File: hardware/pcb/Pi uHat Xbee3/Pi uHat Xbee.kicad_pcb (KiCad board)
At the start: 2 copper layers, 65 x 30.5 mm, 19 parts, among them J1 Conn_01x02, J2 RPi_GPIO, J3 Conn_01x01, J4 Conn_01x01, J5 Conn_01x01, J6 Conn_01x01, J7 Conn_01x01, U1 XBee3

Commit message: Hat Pi Wbee fini
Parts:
- added G***: LOGO, Insa:insa-image, F.Cu at (73.7, 39.4)
- moved R2 46.2 mm to (64.1, 45.7), turned to 270 degrees
- moved D3 42.3 mm to (67.9, 51.4), turned to 90 degrees
- moved R3 37.4 mm to (67.9, 45.7), turned to 270 degrees
- moved R1 36.4 mm to (60.3, 45.7), turned to 270 degrees
- moved D1 35.3 mm to (60.3, 51.4), turned to 90 degrees
- moved D2 33.8 mm to (64.1, 51.4), turned to 90 degrees
- moved J1 23.9 mm to (21.3, 36.6)
- moved J7 19.9 mm to (26.7, 42.5)
- moved C1 12.9 mm to (21.3, 42.7), turned to 270 degrees
- moved J3 10.5 mm to (26.7, 37.5)
- moved J6 10.3 mm to (26.7, 33.0)
- moved J4 8.31 mm to (26.7, 51.4)
- moved J5 7.38 mm to (26.7, 47.0)
- moved U1 6.43 mm to (43.2, 40.6), turned to 0 degrees
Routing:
- net GND: track 0.00 -> 153.5 mm
- net /ASSOCIATE: track 0.00 -> 105.5 mm
- net /~SLEEP: track 0.00 -> 58.3 mm, vias 0 -> 2
- net /SLEEP_REQ: track 0.00 -> 31.3 mm
- net /RSSI_PWM: track 0.00 -> 27.5 mm
- net /DIN: track 0.00 -> 25.2 mm
- net /~RESET: track 0.00 -> 24.8 mm
- net Net-(J2-Pad33): track 0.00 -> 20.3 mm
- net Net-(J2-Pad31): track 0.00 -> 19.0 mm
- net Net-(J2-Pad29): track 0.00 -> 17.8 mm
- net Net-(C1-Pad1): track 0.00 -> 16.2 mm
- net /DOUT: track 0.00 -> 13.0 mm
- net VDD: track 0.00 -> 5.08 mm
- net Net-(D3-Pad2): track 0.00 -> 2.68 mm
- net Net-(D2-Pad2): track 0.00 -> 2.68 mm
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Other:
- board text added: "06/01/2022"
- board text added: "Hat Xbee"
- board text added: "Idd XBEE"
- board text added: "Ver 1.0"

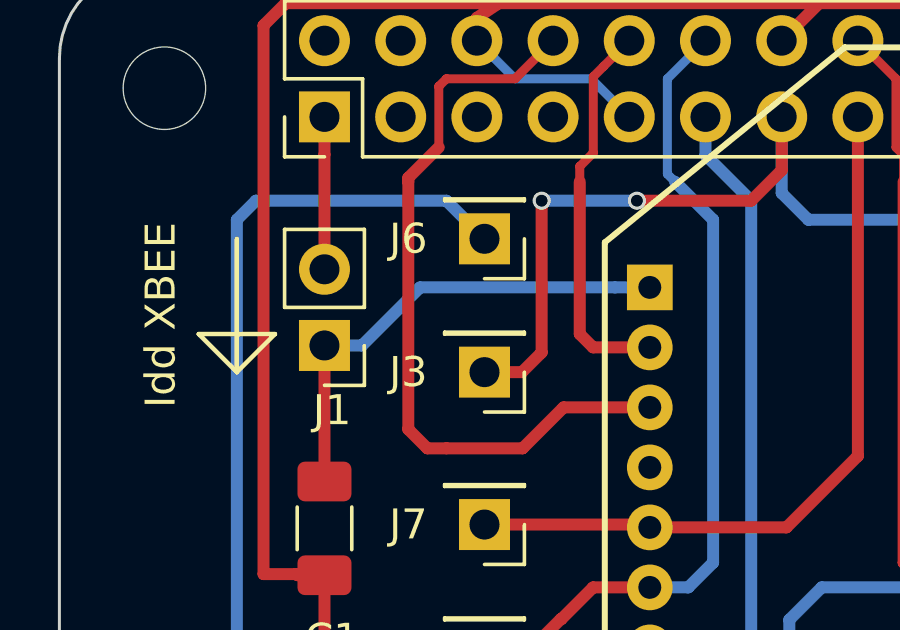
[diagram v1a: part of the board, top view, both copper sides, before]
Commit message: reorganisation de l'arborescence + renommage serveré
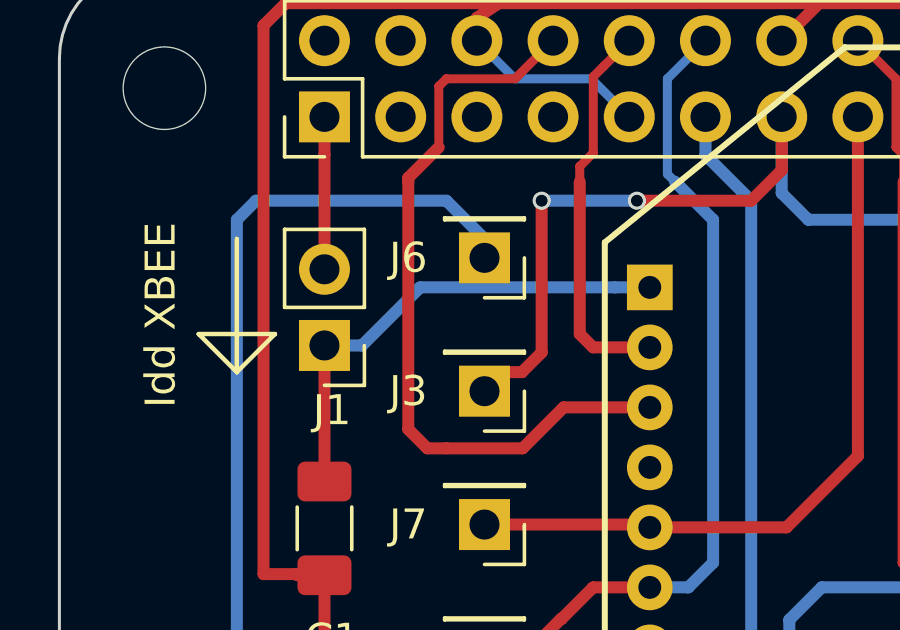
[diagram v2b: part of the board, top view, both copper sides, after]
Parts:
- moved J3 0.63 mm to (26.7, 38.1)
- moved J6 0.63 mm to (26.7, 33.7)
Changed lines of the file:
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@@
   )
   (setup
-    (last_trace_width 0.4)
+    (last_trace_width 0.25)
     (user_trace_width 0.2)
     (user_trace_width 0.25)
@@
     (add_net "Net-(J2-Pad33)")
     (add_net VDD)
+  )
+  (module Insa:Xbee3 locked (layer F.Cu)
+    (at 43.18 40.64)
+    (fp_text reference U1 (at 13.335 -8.89) (layer F.SilkS)
+      (effects (font (size 1 1) (thickness 0.15)))
+    )
+    (fp_text value XBee3 (at 0 6.5) (layer F.Fab)
+      (effects (font (size 1 1) (thickness 0.15)))
+    )
+    (fp_line (start -12.5 -7.5) (end -4.5 -14) (layer F.CrtYd) (width 0.2))
+    (fp_line (start -12.5 13.5) (end -12.5 -7.5) (layer F.CrtYd) (width 0.2))
+    (fp_line (start 12.5 13.5) (end -12.5 13.5) (layer F.CrtYd) (width 0.2))
+    (fp_line (start 12.5 -7.5) (end 12.5 13.5) (layer F.CrtYd) (width 0.2))
+    (fp_line (start 4.5 -14) (end 12.5 -7.5) (layer F.CrtYd) (width 0.2))
+    (fp_line (start -4.5 -14) (end 4.5 -14) (layer F.CrtYd) (width 0.2))
+    (fp_line (start -12.5 -7.5) (end -4.5 -14) (layer F.SilkS) (width 0.2))
+    (fp_line (start 4.5 -14) (end 12.5 -7.5) (layer F.SilkS) (width 0.2))
+    (fp_line (start -4.5 -14) (end 4.5 -14) (layer F.SilkS) (width 0.2))
+    (fp_line (start -12.5 13.5) (end -12.5 -7.5) (layer F.SilkS) (width 0.2))
+    (fp_line (start 12.5 13.5) (end 12.5 -7.5) (layer F.SilkS) (width 0.2))
+    (fp_line (start -12.5 13.5) (end 12.5 13.5) (layer F.SilkS) (width 0.2))
+    (pad 10 thru_hole circle (at -11 12) (size 1.524 1.524) (drill 0.762) (layers *.Cu *.Mask)
+      (net 4 GND))
+    (pad 9 thru_hole circle (at -11 10) (size 1.524 1.524) (drill 0.762) (layers *.Cu *.Mask)
+      (net 11 /SLEEP_REQ))
+    (pad 8 thru_hole circle (at -11 8) (size 1.524 1.524) (drill 0.762) (layers *.Cu *.Mask))
+    (pad 7 thru_hole circle (at -11 6) (size 1.524 1.524) (drill 0.762) (layers *.Cu *.Mask))
+    (pad 6 thru_hole circle (at -11 4) (size 1.524 1.524) (drill 0.762) (layers *.Cu *.Mask)
+      (net 12 /RSSI_PWM))
+    (pad 5 thru_hole circle (at -11 2) (size 1.524 1.524) (drill 0.762) (layers *.Cu *.Mask)
+      (net 14 /~RESET))
+    (pad 11 thru_hole circle (at 11 12) (size 1.524 1.524) (drill 0.762) (layers *.Cu *.Mask))
+    (pad 12 thru_hole circle (at 11 10) (size 1.524 1.524) (drill 0.762) (layers *.Cu *.Mask))
+    (pad 13 thru_hole circle (at 11 8) (size 1.524 1.524) (drill 0.762) (layers *.Cu *.Mask)
+      (net 10 /~SLEEP))
+    (pad 14 thru_hole circle (at 11 6) (size 1.524 1.524) (drill 0.762) (layers *.Cu *.Mask))
+    (pad 15 thru_hole circle (at 11 4) (size 1.524 1.524) (drill 0.762) (layers *.Cu *.Mask)
+      (net 13 /ASSOCIATE))
+    (pad 16 thru_hole circle (at 11 2) (size 1.524 1.524) (drill 0.762) (layers *.Cu *.Mask))
+    (pad 20 thru_hole circle (at 11 -6) (size 1.524 1.524) (drill 0.762) (layers *.Cu *.Mask)
+      (net 4 GND))
+    (pad 19 thru_hole circle (at 11 -4) (size 1.524 1.524) (drill 0.762) (layers *.Cu *.Mask)
+      (net 4 GND))
+    (pad 18 thru_hole circle (at 11 -2) (size 1.524 1.524) (drill 0.762) (layers *.Cu *.Mask)
+      (net 4 GND))
+    (pad 1 thru_hole rect (at -11 -6) (size 1.524 1.524) (drill 0.762) (layers *.Cu *.Mask)
+      (net 5 "Net-(C1-Pad1)"))
+    (pad 2 thru_hole circle (at -11 -4) (size 1.524 1.524) (drill 0.762) (layers *.Cu *.Mask)
+      (net 15 /DOUT))
+    (pad 3 thru_hole circle (at -11 -2) (size 1.524 1.524) (drill 0.762) (layers *.Cu *.Mask)
+      (net 16 /DIN))
+    (pad 17 thru_hole circle (at 11 0) (size 1.524 1.524) (drill 0.762) (layers *.Cu *.Mask)
+      (net 4 GND))
+    (pad 4 thru_hole circle (at -11 0) (size 1.524 1.524) (drill 0.762) (layers *.Cu *.Mask))
+    (model /home/dimercur/kicad/local-packages3d/Insa.3dshapes/XBee_Module_-_ZB_Series_S2C_-_2mW_with_Wire_Antenna_-_XB24CZ7WIT-004_1661764185.214.step
+      (offset (xyz 0 -13.9192 6.680200000000001))
+      (scale (xyz 1 1 1))
+      (rotate (xyz 0 -180 0))
+    )
   )
   (module Insa:insa-image (layer F.Cu)
@@
     )
   )
-  (module Insa:Xbee3 locked (layer F.Cu)
-    (at 43.18 40.64)
-    (fp_text reference U1 (at 13.335 -8.89) (layer F.SilkS)
-      (effects (font (size 1 1) (thickness 0.15)))
-    )
-    (fp_text value XBee3 (at 0 6.5) (layer F.Fab)
-      (effects (font (size 1 1) (thickness 0.15)))
-    )
-    (fp_line (start -12.5 -7.5) (end -4.5 -14) (layer F.CrtYd) (width 0.2))
-    (fp_line (start -12.5 13.5) (end -12.5 -7.5) (layer F.CrtYd) (width 0.2))
-    (fp_line (start 12.5 13.5) (end -12.5 13.5) (layer F.CrtYd) (width 0.2))
-    (fp_line (start 12.5 -7.5) (end 12.5 13.5) (layer F.CrtYd) (width 0.2))
-    (fp_line (start 4.5 -14) (end 12.5 -7.5) (layer F.CrtYd) (width 0.2))
-    (fp_line (start -4.5 -14) (end 4.5 -14) (layer F.CrtYd) (width 0.2))
-    (fp_line (start -12.5 -7.5) (end -4.5 -14) (layer F.SilkS) (width 0.2))
-    (fp_line (start 4.5 -14) (end 12.5 -7.5) (layer F.SilkS) (width 0.2))
-    (fp_line (start -4.5 -14) (end 4.5 -14) (layer F.SilkS) (width 0.2))
-    (fp_line (start -12.5 13.5) (end -12.5 -7.5) (layer F.SilkS) (width 0.2))
-    (fp_line (start 12.5 13.5) (end 12.5 -7.5) (layer F.SilkS) (width 0.2))
-    (fp_line (start -12.5 13.5) (end 12.5 13.5) (layer F.SilkS) (width 0.2))
-    (pad 10 thru_hole circle (at -11 12) (size 1.524 1.524) (drill 0.762) (layers *.Cu *.Mask)
-      (net 4 GND))
-    (pad 9 thru_hole circle (at -11 10) (size 1.524 1.524) (drill 0.762) (layers *.Cu *.Mask)
-      (net 11 /SLEEP_REQ))
-    (pad 8 thru_hole circle (at -11 8) (size 1.524 1.524) (drill 0.762) (layers *.Cu *.Mask))
-    (pad 7 thru_hole circle (at -11 6) (size 1.524 1.524) (drill 0.762) (layers *.Cu *.Mask))
-    (pad 6 thru_hole circle (at -11 4) (size 1.524 1.524) (drill 0.762) (layers *.Cu *.Mask)
-      (net 12 /RSSI_PWM))
-    (pad 5 thru_hole circle (at -11 2) (size 1.524 1.524) (drill 0.762) (layers *.Cu *.Mask)
-      (net 14 /~RESET))
-    (pad 11 thru_hole circle (at 11 12) (size 1.524 1.524) (drill 0.762) (layers *.Cu *.Mask))
-    (pad 12 thru_hole circle (at 11 10) (size 1.524 1.524) (drill 0.762) (layers *.Cu *.Mask))
-    (pad 13 thru_hole circle (at 11 8) (size 1.524 1.524) (drill 0.762) (layers *.Cu *.Mask)
-      (net 10 /~SLEEP))
-    (pad 14 thru_hole circle (at 11 6) (size 1.524 1.524) (drill 0.762) (layers *.Cu *.Mask))
-    (pad 15 thru_hole circle (at 11 4) (size 1.524 1.524) (drill 0.762) (layers *.Cu *.Mask)
-      (net 13 /ASSOCIATE))
-    (pad 16 thru_hole circle (at 11 2) (size 1.524 1.524) (drill 0.762) (layers *.Cu *.Mask))
-    (pad 20 thru_hole circle (at 11 -6) (size 1.524 1.524) (drill 0.762) (layers *.Cu *.Mask)
-      (net 4 GND))
-    (pad 19 thru_hole circle (at 11 -4) (size 1.524 1.524) (drill 0.762) (layers *.Cu *.Mask)
-      (net 4 GND))
-    (pad 18 thru_hole circle (at 11 -2) (size 1.524 1.524) (drill 0.762) (layers *.Cu *.Mask)
-      (net 4 GND))
-    (pad 1 thru_hole rect (at -11 -6) (size 1.524 1.524) (drill 0.762) (layers *.Cu *.Mask)
-      (net 5 "Net-(C1-Pad1)"))
-    (pad 2 thru_hole circle (at -11 -4) (size 1.524 1.524) (drill 0.762) (layers *.Cu *.Mask)
-      (net 15 /DOUT))
-    (pad 3 thru_hole circle (at -11 -2) (size 1.524 1.524) (drill 0.762) (layers *.Cu *.Mask)
-      (net 16 /DIN))
-    (pad 17 thru_hole circle (at 11 0) (size 1.524 1.524) (drill 0.762) (layers *.Cu *.Mask)
-      (net 4 GND))
-    (pad 4 thru_hole circle (at -11 0) (size 1.524 1.524) (drill 0.762) (layers *.Cu *.Mask))
-    (model "/home/dimercur/kicad/local-packages3d/Insa.3dshapes/XBee Pro 60mW.STEP"
-      (offset (xyz -2 7.5 8))
-      (scale (xyz 1 1 1))
-      (rotate (xyz -90 0 -90))
-    )
-  )
   (module Resistor_SMD:R_1206_3216Metric_Pad1.30x1.75mm_HandSolder (layer F.Cu)
     (at 67.945 45.72 270)
@@
   )
   (module Connector_PinHeader_2.54mm:PinHeader_1x01_P2.54mm_Vertical (layer F.Cu)
-    (at 26.67 33.02 180)
+    (at 26.67 33.655 180)
     (descr "Through hole straight pin header, 1x01, 2.54mm pitch, single row")
     (tags "Through hole pin header THT 1x01 2.54mm single row")
@@
   )
   (module Connector_PinHeader_2.54mm:PinHeader_1x01_P2.54mm_Vertical (layer F.Cu)
-    (at 26.67 37.465 180)
+    (at 26.67 38.1 180)
     (descr "Through hole straight pin header, 1x01, 2.54mm pitch, single row")
     (tags "Through hole pin header THT 1x01 2.54mm single row")
